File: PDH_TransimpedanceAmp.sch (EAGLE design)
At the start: 21 parts, among them U1 LMH6626, X1 UMC, X2 UMC

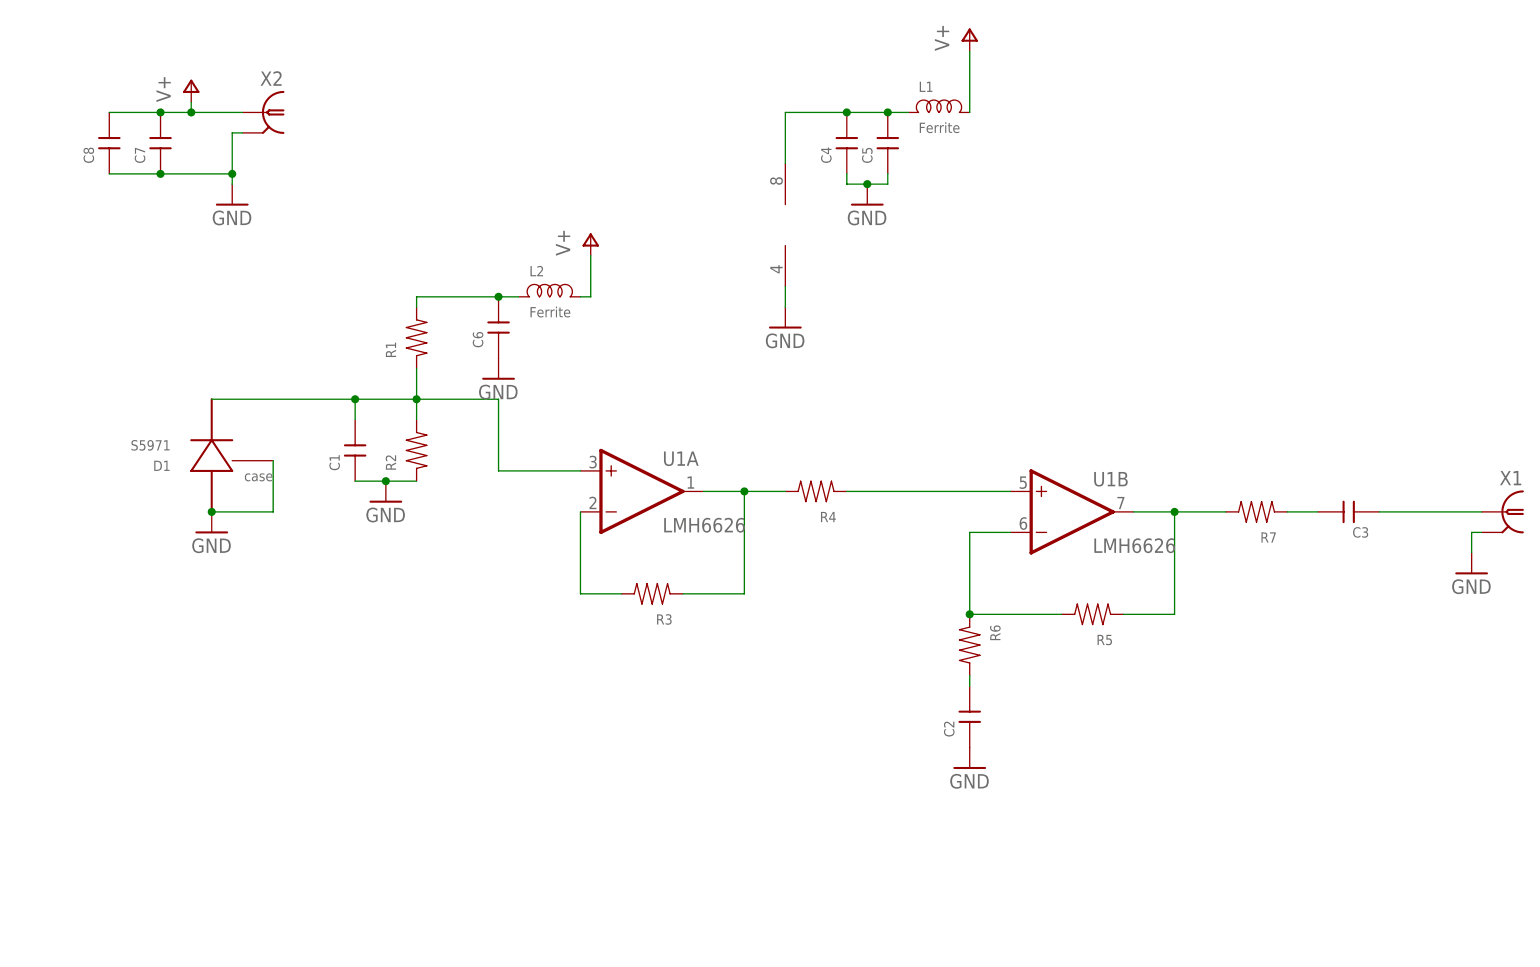
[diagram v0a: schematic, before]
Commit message: schematic and layout done; a little packed so going to reduce filtering caps
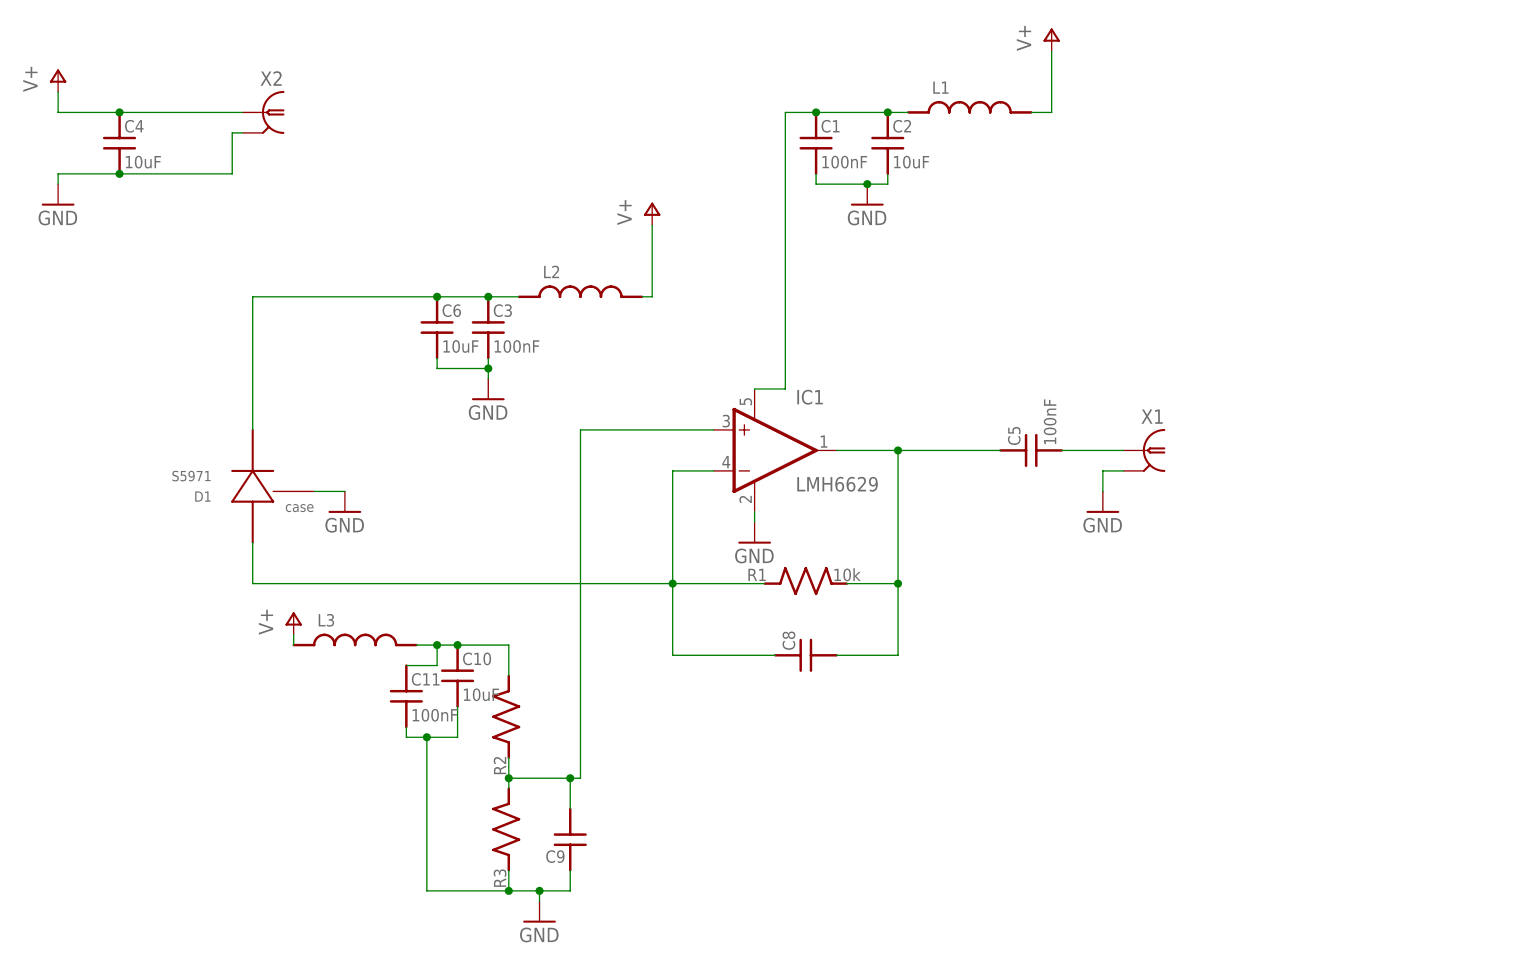
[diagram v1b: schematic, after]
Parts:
- removed C7: (no value), rlc-jqi:CAP0805
- removed R4, R5, R6, R7: (no value), rlc-jqi:RES0402
- removed U1: LMH6626, RF_TransimpedanceAmp:LMH6626
- added C10: 10uF, jqi_passives:C_MLCC_SMDCMLCC_0805
- added C11: 100nF, jqi_passives:C_MLCC_SMDCMLCC_0603
- added C9: (no value), jqi_passives:C_MLCC_SMDCMLCC_0603
- added IC1: LMH6629, opamp-jqi:OPAMP-5PIN-SOT23
- added L3: (no value), jqi_passives:L_FERRITE_SMDLFERRITE_0805
- C1, C3: value (none) -> 100nF; device rlc-jqi:CAP0402 -> jqi_passives:C_MLCC_SMDCMLCC_0603
- C2, C4: value (none) -> 10uF; device rlc-jqi:CAP0402 -> jqi_passives:C_MLCC_SMDCMLCC_0805
- C5: value (none) -> 100nF; device rlc-jqi:CAP0805 -> jqi_passives:C_MLCC_SMDCMLCC_0603
- C6: value (none) -> 10uF; device rlc-jqi:CAP0805 -> jqi_passives:C_MLCC_SMDCMLCC_0805
- C8: device rlc-jqi:CAP0402 -> jqi_passives:C_MLCC_SMDCMLCC_0603
- L1, L2: value Ferrite -> (none); device rlc-jqi:INDUCTOR-0805 -> jqi_passives:L_FERRITE_SMDLFERRITE_0805
- R1: value (none) -> 10k; device rlc-jqi:RES0402 -> jqi_passives:R_SMDR0603
- R2, R3: device rlc-jqi:RES0402 -> jqi_passives:R_SMDR0603
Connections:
- removed net N$5: R3.P$1, R4.P$2, U1A.OUT
- removed net N$6: R4.P$1, U1B.+IN
- removed net N$7: C2.P$2, R6.P$2
- removed net N$8: R5.P$1, R7.P$2, U1B.OUT
- net GND: now also C1.2, C10.2, C11.2, C2.2, C3.2, C4.2, C6.2, C9.1, IC1.V-, R3.1; no longer C1.P$1, C2.P$1, C4.P$1, C5.P$1, C6.P$1, C7.P$1, C8.P$1, D1.ANODE, R2.P$1, U1G$3.V-
- net N$1: now also C8.1, D1.ANODE, IC1.-IN, R1.1; no longer C1.P$2, D1.CATHODE, R1.P$1, R2.P$2, U1A.+IN
- net N$10: now also C1.1, C2.1, IC1.V+, L1.1; no longer C4.P$2, C5.P$2, L1.P$1, U1G$3.V+
- net N$11: now also C5.2; no longer C3.P$1
- net N$2: now also C5.1, C8.2, IC1.OUT, R1.2; no longer R5.P$2, R6.P$1, U1B.-IN
- net N$3: now also C10.1, C11.1, L3.2, R2.2; no longer C3.P$2, R7.P$1
- net N$4: now also C9.2, IC1.+IN, R2.1, R3.2; no longer R3.P$2, U1A.-IN
- net N$9: now also C3.1, C6.1, D1.CATHODE, L2.1; no longer C6.P$2, L2.P$1, R1.P$2
- net V+: now also C4.1, L1.2, L2.2, L3.1; no longer C7.P$2, C8.P$2, L1.P$2, L2.P$2
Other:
- note added: "V+ should be at +5V"
- moved on the sheet: C1, C2, C3, C4, C5, C6, C8, D1, X1

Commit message: Printed; prototyped and seems to be working
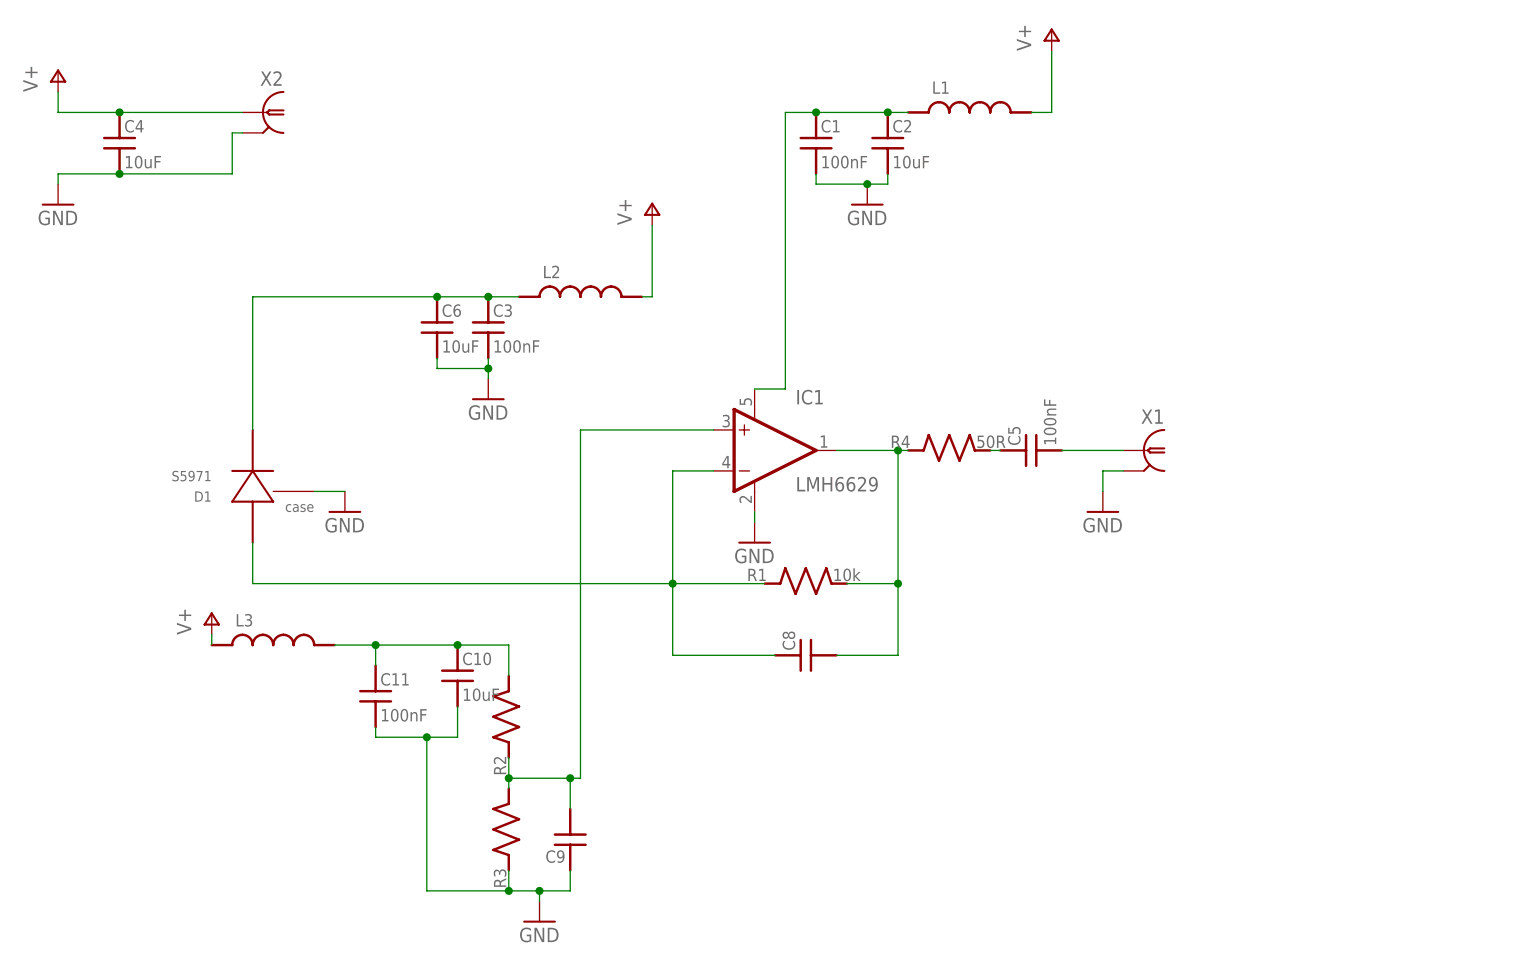
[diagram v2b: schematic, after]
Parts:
- added R4: 50R, jqi_passives:R_SMDR0402
- C1, C11, C3, C5, C8, C9: device jqi_passives:C_MLCC_SMDCMLCC_0603 -> jqi_passives:C_MLCC_SMDCMLCC_0402
- R1, R2, R3: device jqi_passives:R_SMDR0603 -> jqi_passives:R_SMDR0402
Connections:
- new net N$5: C5.1, R4.2
- net N$2: now also R4.1; no longer C5.1
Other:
- note added: "want ~ 1.1pF; start with 490-6208-1-ND"
- moved on the sheet: C11, L3
